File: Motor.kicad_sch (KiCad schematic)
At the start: 3 parts, among them J1 Motor, Q1 NMOS

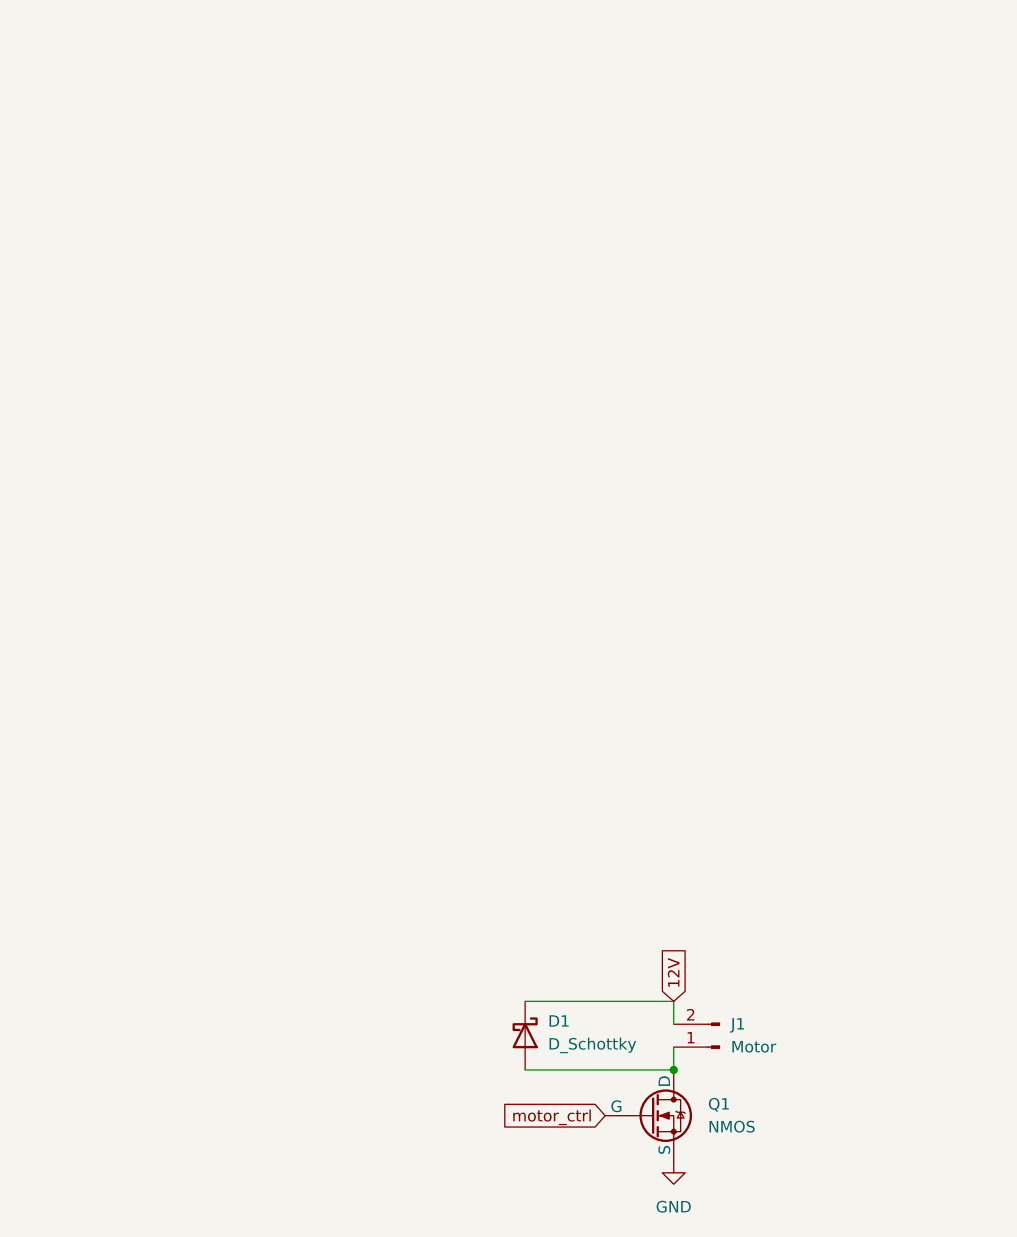
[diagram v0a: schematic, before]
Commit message: Overhaul
Overhauled the schematic so all the components are correct, rewired power to be 12 V instead of 9 V and connected hierarchical labels between modules. Added more decoupling capacitors where they were missing.
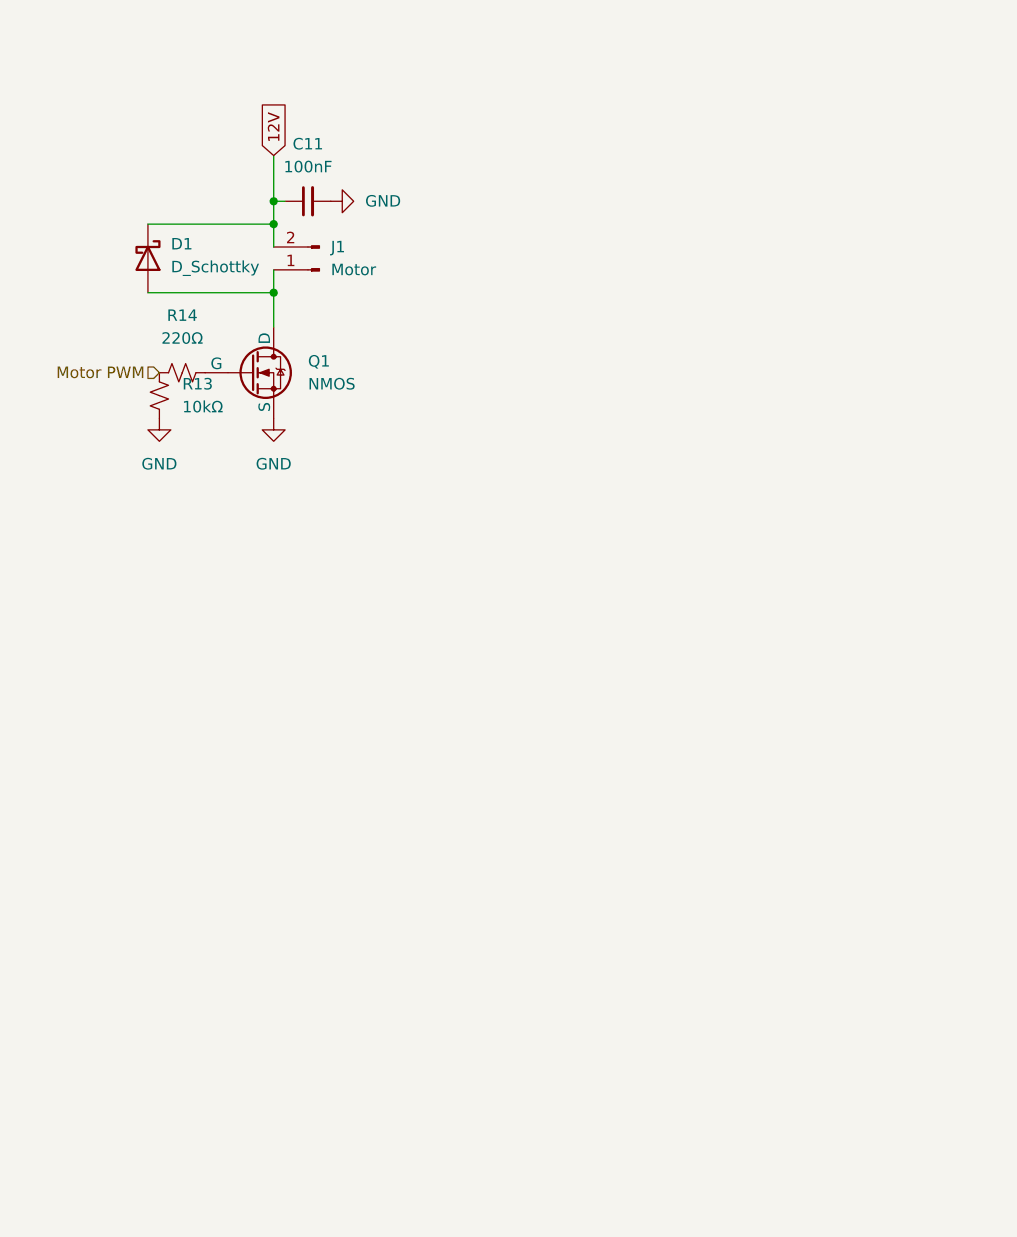
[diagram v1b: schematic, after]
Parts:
- added C11: 100nF, symbol Device:C_Small
- added R13: 10kΩ, symbol Device:R_Small_US
- added R14: 220Ω, symbol Device:R_Small_US
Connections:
- net 12V: now also C11.1
- net GND: now also C11.2, R13.1
- net motor_ctrl: no longer names the net of Q1.2 (G)
- net motor_ctrl: now also R14.2
- new net Motor PWM: R13.2, R14.1
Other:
- moved on the sheet: D1, J1, Q1

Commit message: Clean up
Minor fixes to mistakes in the schematic
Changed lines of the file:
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@@
+	)
+	(junction
+		(at 27.94 46.99)
+		(diameter 0)
+		(color 0 0 0 0)
 	)
 	(junction
@@
 		(pts
 			(xy 40.64 27.94) (xy 40.64 30.48)
+		)
+		(stroke
+			(width 0)
+			(type default)
+		)
+	)
+	(wire
+		(pts
+			(xy 26.67 46.99) (xy 27.94 46.99)
 		)
 		(stroke
@@
 	(hierarchical_label "Motor PWM"
 		(shape input)
-		(at 27.94 46.99 180)
+		(at 26.67 46.99 180)
 		(effects
 			(font

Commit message: Gave footprints to everything
Footprints
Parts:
- C11: footprint (none) -> Capacitor_SMD:C_0603_1608Metric
- D1: footprint (none) -> Diode_SMD:D_SOD-123
- J1: footprint (none) -> TerminalBlock_Altech:Altech_AK100_1x02_P5.00mm
- Q1: footprint (none) -> Package_SO:SO-8_3.9x4.9mm_P1.27mm
- R13, R14: footprint (none) -> Resistor_SMD:R_0603_1608Metric
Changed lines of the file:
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@@
 			)
 		)
-		(property "Footprint" ""
+		(property "Footprint" "Package_SO:SO-8_3.9x4.9mm_P1.27mm"
 			(at 43.18 44.45 0)
 			(hide yes)
@@
 			)
 		)
-		(property "Footprint" ""
+		(property "Footprint" "Resistor_SMD:R_0603_1608Metric"
 			(at 30.48 46.99 0)
 			(hide yes)
@@
 			)
 		)
-		(property "Footprint" ""
+		(property "Footprint" "TerminalBlock_Altech:Altech_AK100_1x02_P5.00mm"
 			(at 45.72 35.56 0)
 			(hide yes)
@@
 			)
 		)
-		(property "Footprint" ""
+		(property "Footprint" "Resistor_SMD:R_0603_1608Metric"
 			(at 27.94 49.53 0)
 			(hide yes)
@@
 			)
 		)
-		(property "Footprint" ""
+		(property "Footprint" "Diode_SMD:D_SOD-123"
 			(at 26.67 34.29 0)
 			(hide yes)
@@
 			)
 		)
-		(property "Footprint" ""
+		(property "Footprint" "Capacitor_SMD:C_0603_1608Metric"
 			(at 44.45 27.94 0)
 			(hide yes)

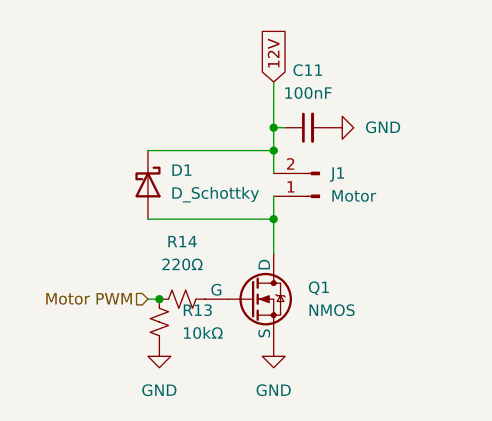
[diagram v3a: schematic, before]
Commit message: USB-C + Complete wiring
Compltetly wired the pcb (I don't understand the DRC errors) and added a usb C to flash the stm, modified the switch to be the BOOT0 for the stm so it controls whether the stm is in flash mode
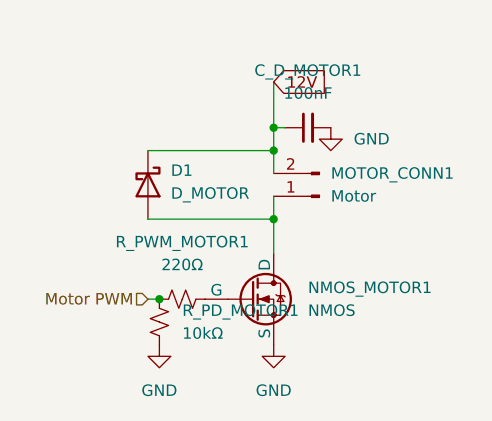
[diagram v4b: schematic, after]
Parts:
- D1: value D_Schottky -> D_MOTOR
- MOTOR_CONN1: renamed from J1; footprint TerminalBlock_Altech:Altech_AK100_1x02_P5.00mm -> TerminalBlock_Phoenix:TerminalBlock_Phoenix_MKDS-1,5-2-5.08_1x02_P5.08mm_Horizontal
- NMOS_MOTOR1: renamed from Q1; footprint Package_SO:SO-8_3.9x4.9mm_P1.27mm -> Package_TO_SOT_SMD:SOT-23_Handsoldering
- renumbered C11 to C_D_MOTOR1, R13 to R_PD_MOTOR1, R14 to R_PWM_MOTOR1
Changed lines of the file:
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@@
 	(global_label "12V"
 		(shape input)
-		(at 40.64 22.86 90)
+		(at 40.64 22.86 0)
 		(fields_autoplaced yes)
 		(effects
@@
 		)
 		(property "Intersheetrefs" "${INTERSHEET_REFS}"
-			(at 40.64 16.3672 90)
+			(at 47.1328 22.86 0)
 			(hide yes)
 			(show_name no)
@@
 		(dnp no)
 		(fields_autoplaced yes)
-		(property "Reference" "Q1"
+		(property "Reference" "NMOS_MOTOR1"
 			(at 44.45 45.7199 0)
 			(show_name no)
@@
 			)
 		)
-		(property "Footprint" "Package_SO:SO-8_3.9x4.9mm_P1.27mm"
+		(property "Footprint" "Package_TO_SOT_SMD:SOT-23_Handsoldering"
 			(at 43.18 44.45 0)
 			(hide yes)
@@
 			(project "X19-Float-Board"
 				(path "/00000000-0000-0000-0000-000060e6118b/9d43548c-72e6-48dc-8947-3d07e1d2f4c8"
-					(reference "Q1")
+					(reference "NMOS_MOTOR1")
 					(unit 1)
 				)
@@
 		(dnp no)
 		(fields_autoplaced yes)
-		(property "Reference" "R14"
+		(property "Reference" "R_PWM_MOTOR1"
 			(at 30.48 40.64 90)
 			(show_name no)
@@
 			(project "X19-Float-Board"
 				(path "/00000000-0000-0000-0000-000060e6118b/9d43548c-72e6-48dc-8947-3d07e1d2f4c8"
-					(reference "R14")
+					(reference "R_PWM_MOTOR1")
 					(unit 1)
 				)
@@
 		(dnp no)
 		(fields_autoplaced yes)
-		(property "Reference" "J1"
+		(property "Reference" "MOTOR_CONN1"
 			(at 46.99 33.0199 0)
 			(show_name no)
@@
 			)
 		)
-		(property "Footprint" "TerminalBlock_Altech:Altech_AK100_1x02_P5.00mm"
+		(property "Footprint" "TerminalBlock_Phoenix:TerminalBlock_Phoenix_MKDS-1,5-2-5.08_1x02_P5.08mm_Horizontal"
 			(at 45.72 35.56 0)
 			(hide yes)
@@
 			(project "X19-Float-Board"
 				(path "/00000000-0000-0000-0000-000060e6118b/9d43548c-72e6-48dc-8947-3d07e1d2f4c8"
-					(reference "J1")
+					(reference "MOTOR_CONN1")
 					(unit 1)
 				)
@@
 		(dnp no)
 		(fields_autoplaced yes)
-		(property "Reference" "R13"
+		(property "Reference" "R_PD_MOTOR1"
 			(at 30.48 48.2599 0)
 			(show_name no)
@@
 			(project "X19-Float-Board"
 				(path "/00000000-0000-0000-0000-000060e6118b/9d43548c-72e6-48dc-8947-3d07e1d2f4c8"
-					(reference "R13")
+					(reference "R_PD_MOTOR1")
 					(unit 1)
 				)
@@
 	(symbol
 		(lib_id "power:GND")
-		(at 46.99 27.94 90)
+		(at 46.99 27.94 0)
 		(unit 1)
 		(body_style 1)
@@
 		(fields_autoplaced yes)
 		(property "Reference" "#PWR012"
-			(at 53.34 27.94 0)
+			(at 46.99 34.29 0)
 			(hide yes)
 			(show_name no)
@@
 		)
 		(property "Value" "GND"
-			(at 50.8 27.9399 90)
-			(show_name no)
-			(do_not_autoplace no)
-			(effects
-				(font
-					(size 1.27 1.27)
-				)
-				(justify right)
+			(at 49.53 29.2099 0)
+			(show_name no)
+			(do_not_autoplace no)
+			(effects
+				(font
+					(size 1.27 1.27)
+				)
+				(justify left)
 			)
 		)
@@
 			)
 		)
-		(property "Value" "D_Schottky"
+		(property "Value" "D_MOTOR"
 			(at 29.21 35.2424 90)
 			(show_name no)
@@
 		(dnp no)
 		(fields_autoplaced yes)
-		(property "Reference" "C11"
+		(property "Reference" "C_D_MOTOR1"
 			(at 44.4563 21.59 90)
 			(show_name no)
@@
 			(project "X19-Float-Board"
 				(path "/00000000-0000-0000-0000-000060e6118b/9d43548c-72e6-48dc-8947-3d07e1d2f4c8"
-					(reference "C11")
-					(unit 1)
-				)
+					(reference "C_D_MOTOR1")
+					(unit 1)
+				)

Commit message: Checkpoint
Checkpoint, pre battery telemetry, pre new stm
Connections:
- net 12V renamed 12 V
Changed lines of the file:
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@@
 		)
 	)
-	(global_label "12V"
+	(global_label "12 V"
 		(shape input)
 		(at 40.64 22.86 0)
@@
 		)
 		(property "Intersheetrefs" "${INTERSHEET_REFS}"
-			(at 47.1328 22.86 0)
+			(at 48.1004 22.86 0)
 			(hide yes)
 			(show_name no)

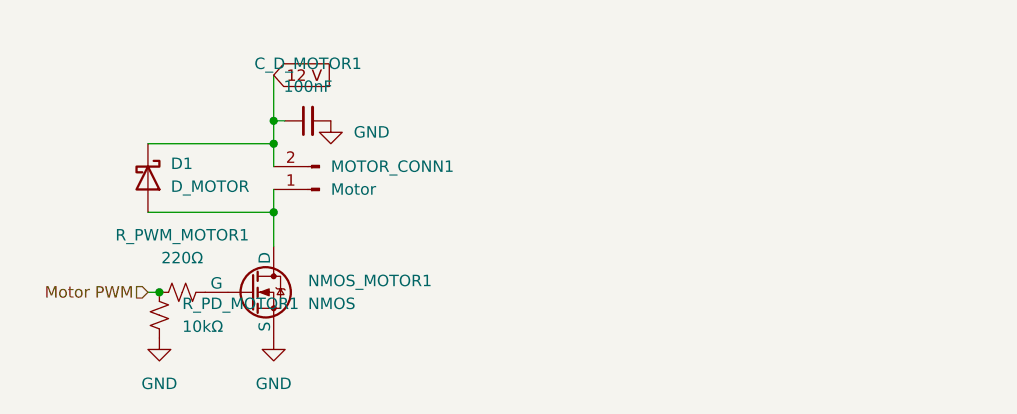
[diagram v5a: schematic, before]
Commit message: Updated Schematic
Updated schematic
Cleaned up dense portions
added H bridge
correct i2c wiring
added ferrite beads
added 12 V power monitoring
added stlink
added power mux
added power from usb
reformatted hierarichal sheets
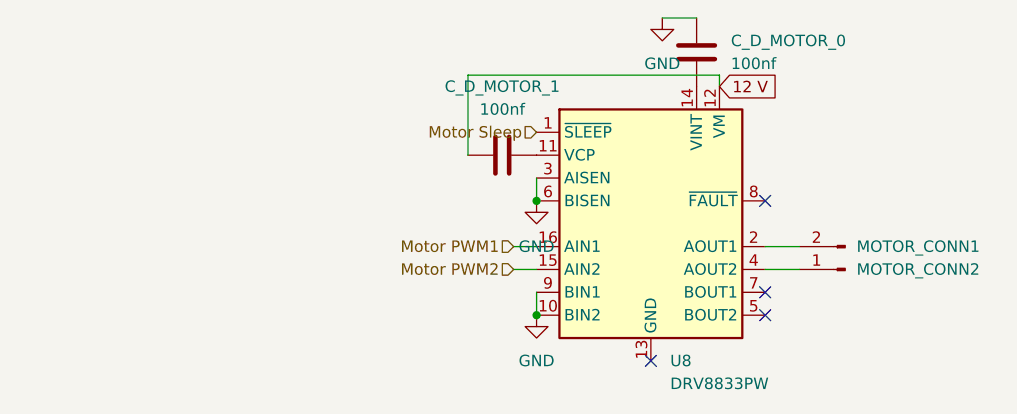
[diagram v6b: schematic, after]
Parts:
- removed C_D_MOTOR1: 100nF, Capacitor_SMD:C_0603_1608Metric, symbol Device:C_Small
- removed D1: D_MOTOR, Diode_SMD:D_SOD-123, symbol Device:D_Schottky
- removed NMOS_MOTOR1: NMOS, Package_TO_SOT_SMD:SOT-23_Handsoldering, symbol Simulation_SPICE:NMOS
- removed R_PD_MOTOR1: 10kΩ, Resistor_SMD:R_0603_1608Metric, symbol Device:R_Small_US
- removed R_PWM_MOTOR1: 220Ω, Resistor_SMD:R_0603_1608Metric, symbol Device:R_Small_US
- added C_D_MOTOR_0, C_D_MOTOR_1: 100nf, symbol Device:C
- added U8: DRV8833PW, Package_SO:TSSOP-16_4.4x5mm_P0.65mm, symbol Driver_Motor:DRV8833PW
- MOTOR_CONN1: value Motor -> MOTOR_CONN2
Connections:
- net 12 V: now also C_D_MOTOR_1.1, U8.12 (VM); no longer MOTOR_CONN1.2 (Pin_2)
- net GND: now also C_D_MOTOR_0.1, U8.10 (BIN2), U8.3 (AISEN), U8.6 (BISEN), U8.9 (BIN1)
- net at MOTOR_CONN1.1 (Pin_1): now also U8.4 (AOUT2)
- new net: C_D_MOTOR_0.2, U8.14 (VINT)
- new net: C_D_MOTOR_1.2, U8.11 (VCP)
- new net: MOTOR_CONN1.2 (Pin_2), U8.2 (AOUT1)
- new net Motor PWM1: U8.16 (AIN1)
- new net Motor PWM2: U8.15 (AIN2)
- new net Motor Sleep: U8.1 (~{SLEEP})
- no-connect marks 0 -> 4

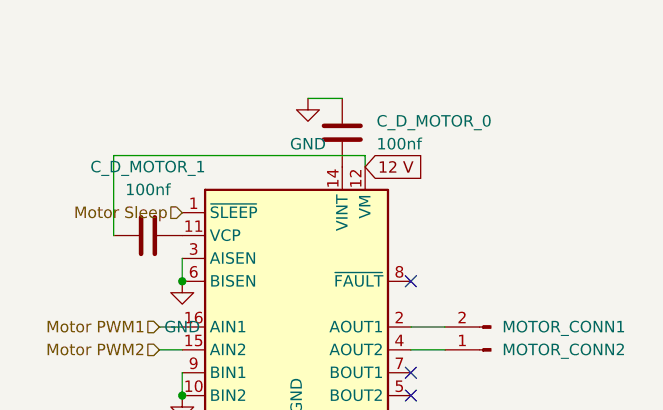
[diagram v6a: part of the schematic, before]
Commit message: USB, TVS, LDO, Passives, I2C
applied changes to usb circuitry, tvs, ldo, passibes and i2c.
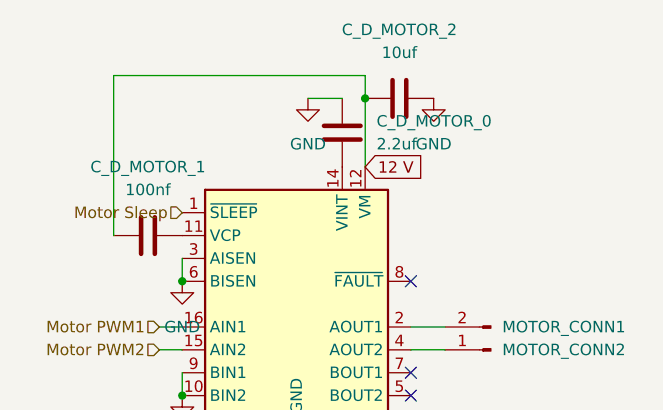
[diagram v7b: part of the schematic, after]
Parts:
- added C_D_MOTOR_2: 10uf, symbol Device:C
- C_D_MOTOR_0: value 100nf -> 2.2uf
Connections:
- net 12 V: now also C_D_MOTOR_2.1
- net GND: now also C_D_MOTOR_2.2
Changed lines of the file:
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@@
 	(paper "A4")
+	(junction
+		(at 90.17 16.51)
+		(diameter 0)
+		(color 0 0 0 0)
+	)
 	(junction
 		(at 69.85 49.53)
@@
 	(wire
 		(pts
-			(xy 90.17 22.86) (xy 90.17 24.13)
+			(xy 90.17 13.97) (xy 90.17 16.51)
+		)
+		(stroke
+			(width 0)
+			(type default)
+		)
+	)
+	(wire
+		(pts
+			(xy 90.17 16.51) (xy 90.17 24.13)
 		)
 		(stroke
@@
 	(wire
 		(pts
-			(xy 62.23 22.86) (xy 62.23 31.75)
-		)
-		(stroke
-			(width 0)
-			(type default)
-		)
-	)
-	(wire
-		(pts
-			(xy 62.23 22.86) (xy 90.17 22.86)
+			(xy 62.23 13.97) (xy 62.23 31.75)
+		)
+		(stroke
+			(width 0)
+			(type default)
+		)
+	)
+	(wire
+		(pts
+			(xy 62.23 13.97) (xy 90.17 13.97)
 		)
 		(stroke
@@
 	)
 	(symbol
+		(lib_id "power:GND")
+		(at 97.79 16.51 0)
+		(unit 1)
+		(body_style 1)
+		(exclude_from_sim no)
+		(in_bom yes)
+		(on_board yes)
+		(in_pos_files yes)
+		(dnp no)
+		(fields_autoplaced yes)
+		(property "Reference" "#PWR037"
+			(at 97.79 22.86 0)
+			(hide yes)
+			(show_name no)
+			(do_not_autoplace no)
+			(effects
+				(font
+					(size 1.27 1.27)
+				)
+			)
+		)
+		(property "Value" "GND"
+			(at 97.79 21.59 0)
+			(show_name no)
+			(do_not_autoplace no)
+			(effects
+				(font
+					(size 1.27 1.27)
+				)
+			)
+		)
+		(property "Footprint" ""
+			(at 97.79 16.51 0)
+			(hide yes)
+			(show_name no)
+			(do_not_autoplace no)
+			(effects
+				(font
+					(size 1.27 1.27)
+				)
+			)
+		)
+		(property "Datasheet" ""
+			(at 97.79 16.51 0)
+			(hide yes)
+			(show_name no)
+			(do_not_autoplace no)
+			(effects
+				(font
+					(size 1.27 1.27)
+				)
+			)
+		)
+		(property "Description" "Power symbol creates a global label with name \"GND\" , ground"
+			(at 97.79 16.51 0)
+			(hide yes)
+			(show_name no)
+			(do_not_autoplace no)
+			(effects
+				(font
+					(size 1.27 1.27)
+				)
+			)
+		)
+		(pin "1"
+		)
+		(instances
+			(project "X19-Float-Board"
+				(path "/00000000-0000-0000-0000-000060e6118b/9d43548c-72e6-48dc-8947-3d07e1d2f4c8"
+					(reference "#PWR037")
+					(unit 1)
+				)
+			)
+		)
+	)
+	(symbol
 		(lib_id "Device:C")
 		(at 87.63 20.32 0)
@@
 			)
 		)
-		(property "Value" "100nf"
+		(property "Value" "2.2uf"
 			(at 91.44 21.5899 0)
 			(show_name no)
@@
 					(unit 1)
 				)
+			)
+		)
+	)
+	(symbol
+		(lib_id "Device:C")
+		(at 93.98 16.51 90)
+		(unit 1)
+		(body_style 1)
+		(exclude_from_sim no)
+		(in_bom yes)
+		(on_board yes)
+		(in_pos_files yes)
+		(dnp no)
+		(fields_autoplaced yes)
+		(property "Reference" "C_D_MOTOR_2"
+			(at 93.98 8.89 90)
+			(show_name no)
+			(do_not_autoplace no)
+			(effects
+				(font
+					(size 1.27 1.27)
+				)
+			)
+		)
+		(property "Value" "10uf"
+			(at 93.98 11.43 90)
+			(show_name no)
+			(do_not_autoplace no)
+			(effects
+				(font
+					(size 1.27 1.27)
+				)
+			)
+		)
+		(property "Footprint" ""
+			(at 97.79 15.5448 0)
+			(hide yes)
+			(show_name no)
+			(do_not_autoplace no)
+			(effects
+				(font
+					(size 1.27 1.27)
+				)
+			)
+		)
+		(property "Datasheet" ""
+			(at 93.98 16.51 0)
+			(hide yes)
+			(show_name no)
+			(do_not_autoplace no)
+			(effects
+				(font
+					(size 1.27 1.27)
+				)
+			)
+		)
+		(property "Description" "Unpolarized capacitor"
+			(at 93.98 16.51 0)
+			(hide yes)
+			(show_name no)
+			(do_not_autoplace no)
+			(effects
+				(font
+					(size 1.27 1.27)
+				)
+			)
+		)
+		(pin "2"
+		)
+		(pin "1"
+		)
+		(instances
+			(project "X19-Float-Board"
+				(path "/00000000-0000-0000-0000-000060e6118b/9d43548c-72e6-48dc-8947-3d07e1d2f4c8"
+					(reference "C_D_MOTOR_2")
+					(unit 1)
+				)
